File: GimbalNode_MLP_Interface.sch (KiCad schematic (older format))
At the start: 17 parts

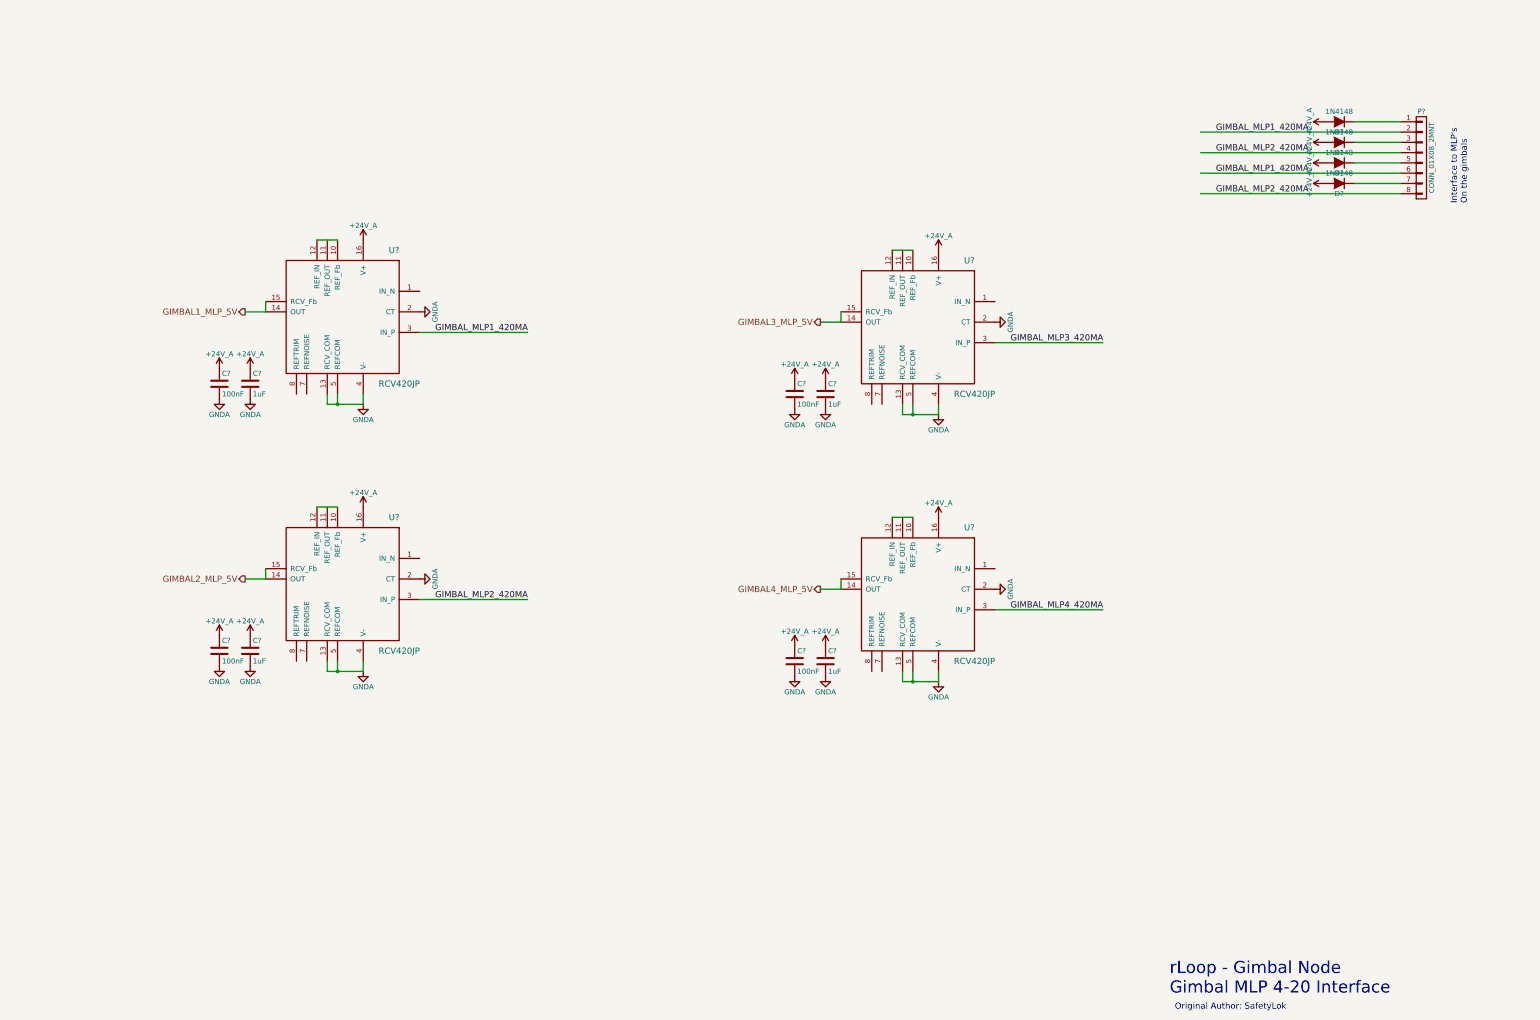
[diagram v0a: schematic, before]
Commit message: Fixup various caps on 4-20ma sheet.
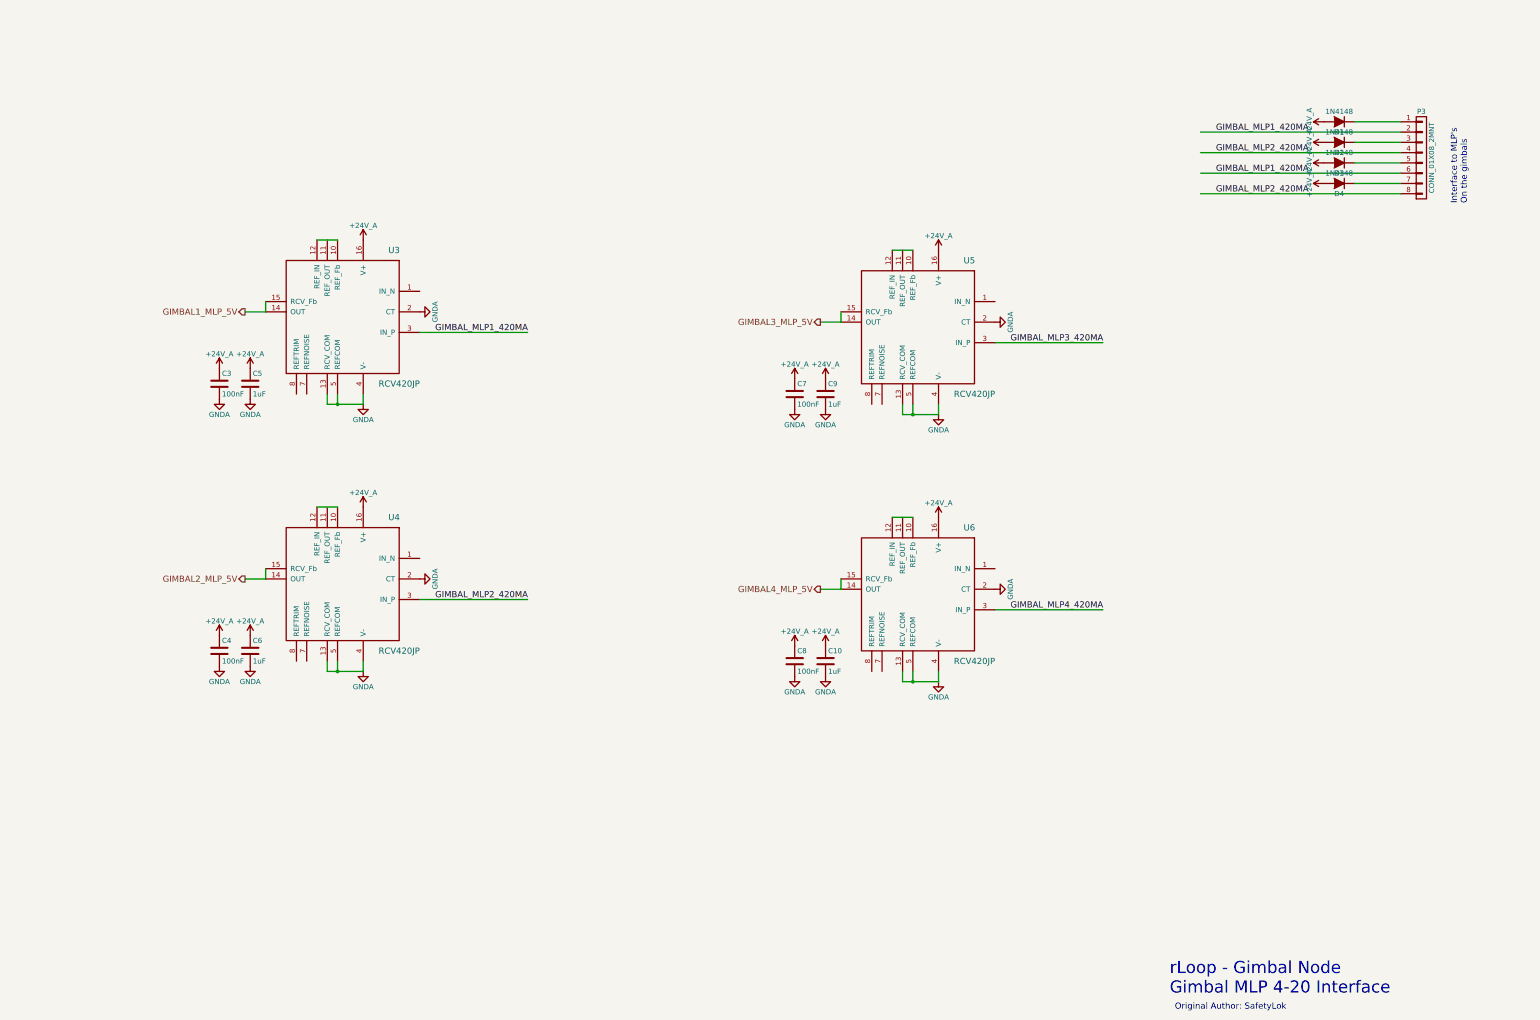
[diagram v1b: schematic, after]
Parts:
- gave numbers to parts that had none: 17

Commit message: Fixup 5V to 3V connections
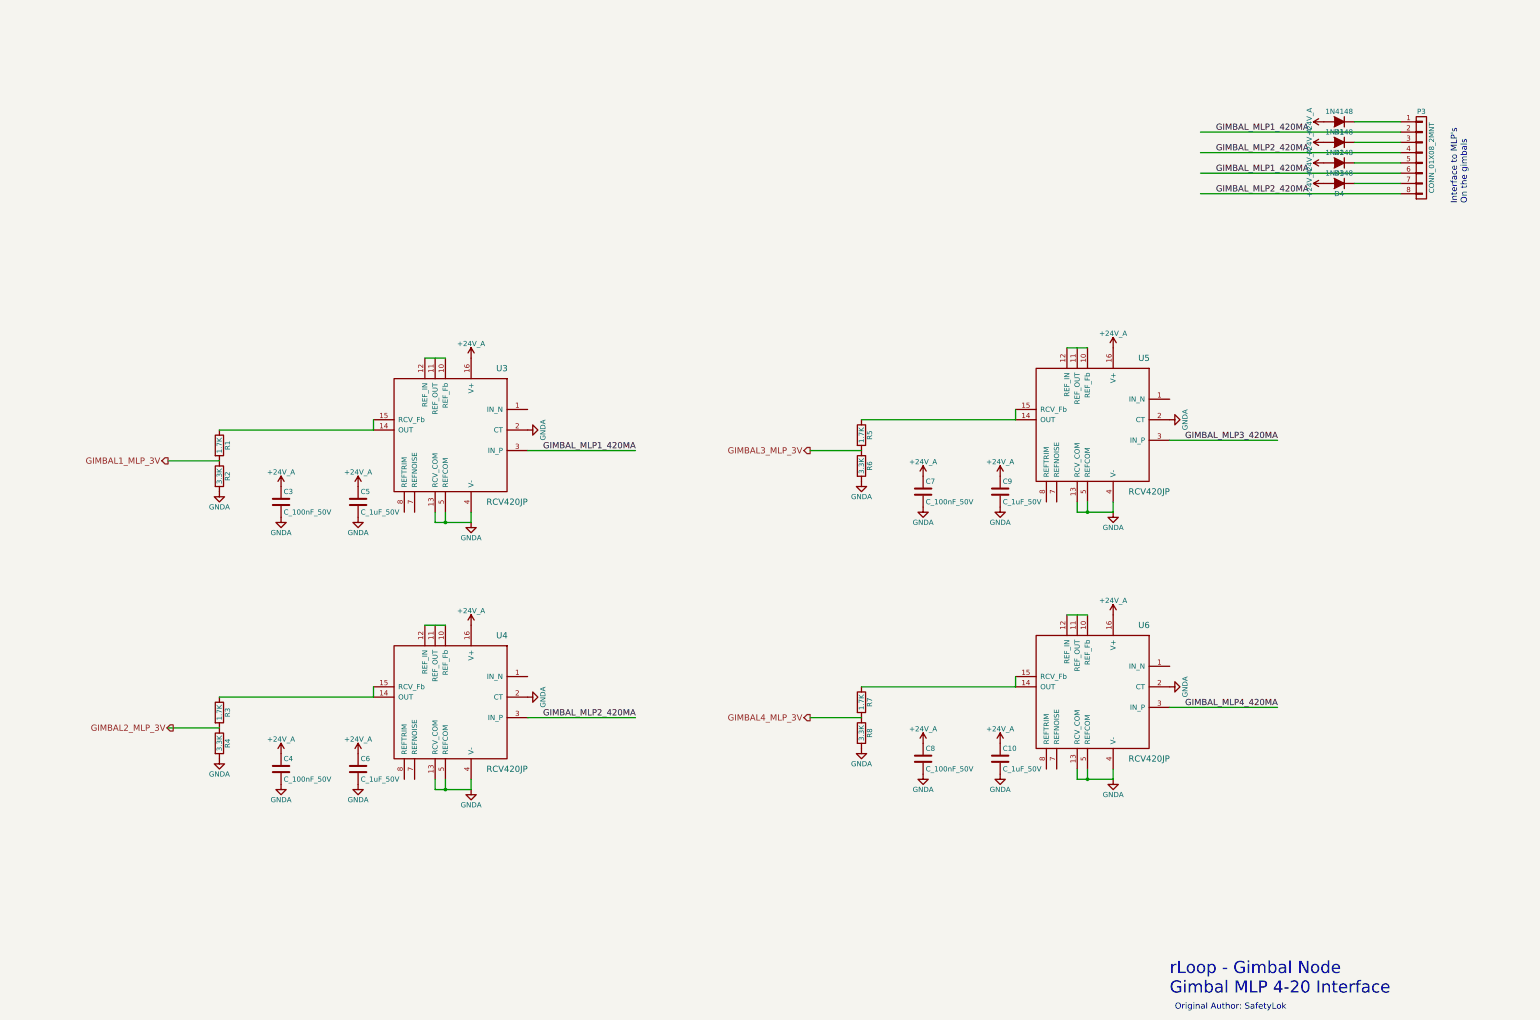
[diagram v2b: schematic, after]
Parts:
- removed C10, C5, C6, C9: 1uF, symbol C
- removed C3, C4, C7, C8: 100nF, symbol C
- added C10, C5, C6, C9: C_1uF_50V, RLOOP_FOOTPRINTS:rLoop_C_0603, symbol C_1uF_50V
- added C3, C4, C7, C8: C_100nF_50V, RLOOP_FOOTPRINTS:rLoop_C_0603, symbol C_100nF_50V
- added R1, R3, R5, R7: 1.7K, RLOOP_FOOTPRINTS:rLoop_R_0603, symbol 1.7K
- added R2, R4, R6, R8: 3.3K, RLOOP_FOOTPRINTS:rLoop_R_0603, symbol 3.3K
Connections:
- net labels added: GIMBAL1_MLP_3V, GIMBAL2_MLP_3V, GIMBAL3_MLP_3V, GIMBAL4_MLP_3V
- net labels removed: GIMBAL1_MLP_5V, GIMBAL2_MLP_5V, GIMBAL3_MLP_5V, GIMBAL4_MLP_5V
- wire segments 40 -> 44
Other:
- moved on the sheet: U3, U4, U5, U6

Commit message: Update connectors, diodes, add zener's and anotate.
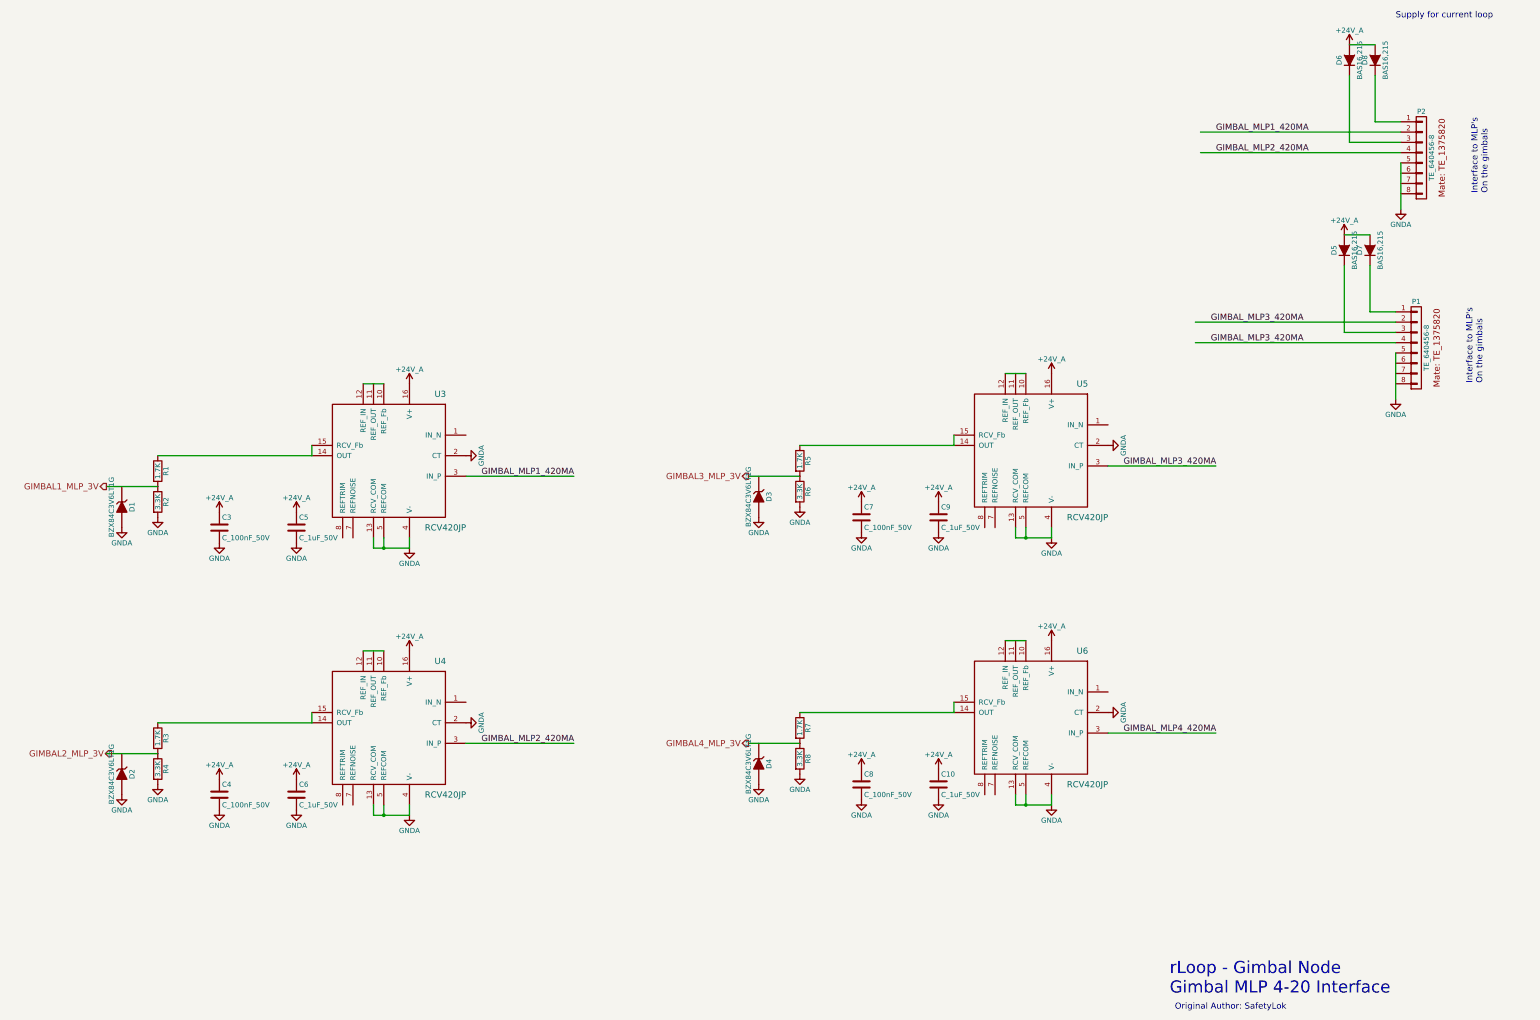
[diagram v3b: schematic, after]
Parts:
- removed D1, D2, D3, D4: 1N4148, symbol D
- removed P3: CONN_01X08_2MNT, symbol CONN_01X08_2MNT
- added D1, D2, D3, D4: BZX84C3V6LT1G, RLOOP_FOOTPRINTS:rLoop_SOT23, symbol BZX84C3V6LT1G
- added D5, D6, D7, D8: BAS16,215, RLOOP_FOOTPRINTS:rLoop_SOT23, symbol BAS16,215
- added P1, P2: TE_640456-8, RLOOP_FOOTPRINTS:rLoop_TE640456-8, symbol TE_640456-8
- U3, U4, U5, U6: footprint (none) -> RLOOP_FOOTPRINTS:rLoop_DIP16
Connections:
- wire segments 44 -> 52
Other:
- note added: "Supply for current loop"
- moved on the sheet: C10, C3, C4, C5, C6, C7, C8, C9, R1, R2, R3, R4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
